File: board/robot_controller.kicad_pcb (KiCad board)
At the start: 2 copper layers, 171.4 x 142.6 mm, 328 parts, among them J101 +3.3V, J102 +24V, J103 GND, J104 JTAG-ARM, J105 Power, J106 FTDI-USB, J107 Industrial Inputs, J108 Industrial Outputs, J109 MCU-USB, J110 AUX-USART6, J111 UEXT0, J112 UEXT1, J113 RGB LEDs, J201 Temp 0, J2301 Motor 0, J2302 Limit 0, J2401 Motor 1, J2402 Limit 1, J2501 Motor 2, J2502 Limit 2, J2601 Motor 3, J2602 Limit 3, J301 Temp 1, Q101 PNP, Q1501 NJT4031NT1G, Q1601 NJT4031NT1G, Q1701 NJT4031NT1G, Q1801 NJT4031NT1G, Q1901 NJT4031NT1G, Q2001 NJT4031NT1G, Q2101 NJT4031NT1G, Q2201 NJT4031NT1G, Q401 MMBT5962, Q402 MMBT5962, Q501 MMBT5962, Q502 MMBT5962, SW101 SW0, SW102 SW1, SW103 SW2, SW104 SW3, SW105 RESET, SW106 BOOT, U101 STM32F405-144, U102 FT232RL, U201 MAX6675, U2301 L6470, U2401 L6470, U2501 L6470, U2601 L6470, U301 MAX6675, U601 LMZ14201, X101 8MHZ

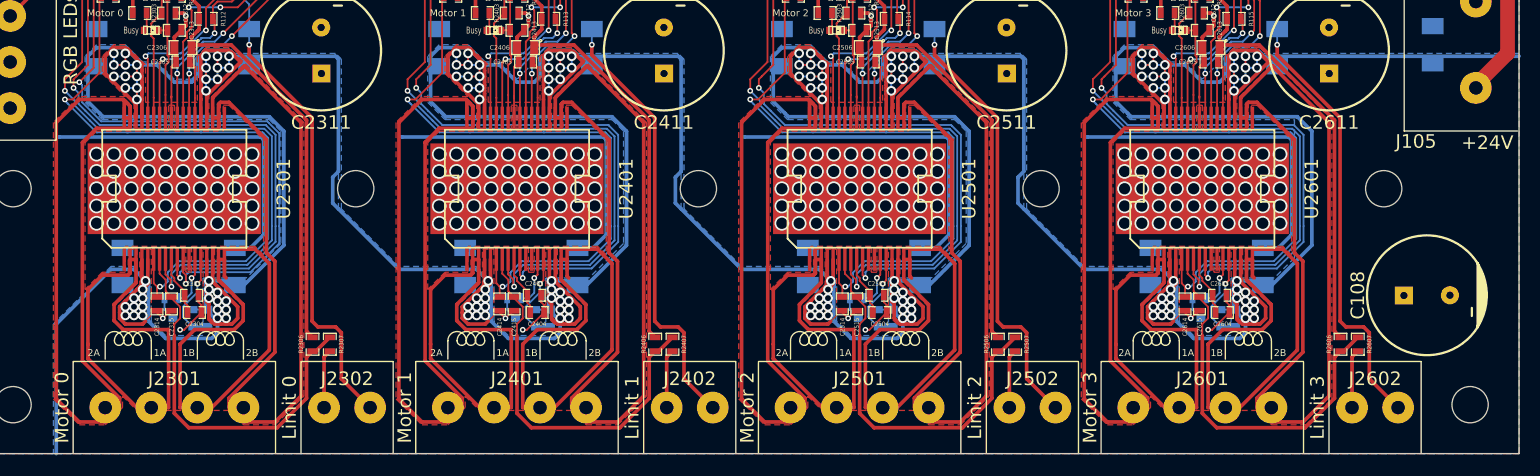
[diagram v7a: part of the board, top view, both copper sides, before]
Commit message: PentaLogix DRC Fixes
Moved some traces inside of the board outline.
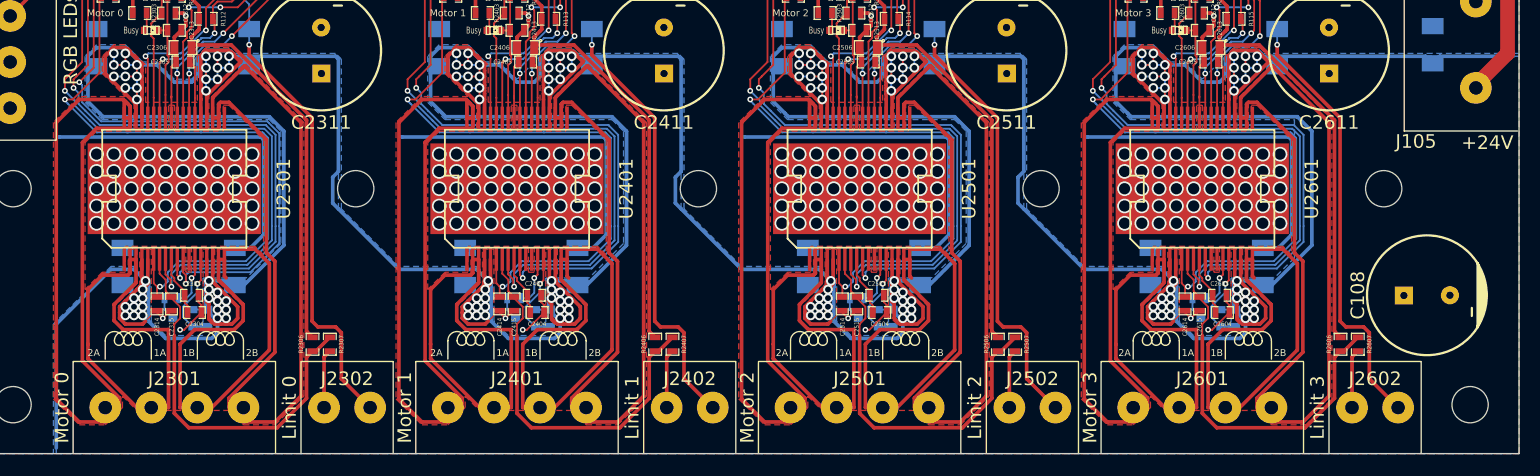
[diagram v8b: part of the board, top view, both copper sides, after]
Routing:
- net +24V: track 1244.9 -> 1244.3 mm
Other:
- rule pad_to_mask_clearance: 0.1016 -> 0.0254
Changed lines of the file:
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@@
-(kicad_pcb (version 3) (host pcbnew "(2014-02-15 BZR 4701)-product")
+(kicad_pcb (version 3) (host pcbnew "(2014-01-30 BZR 4648)-product")
   (general
     (links 796)
-    (no_connects 181)
-    (area -3.24213 15.8496 210.185001 162.46348)
+    (no_connects 0)
+    (area -3.24213 15.8496 208.98213 162.46348)
     (thickness 1.6)
     (drawings 59)
-    (tracks 4551)
+    (tracks 4554)
     (zones 0)
     (modules 328)
@@
   )
   (setup
-    (last_trace_width 0.2032)
+    (last_trace_width 0.4064)
     (user_trace_width 0.2032)
     (user_trace_width 0.4064)
@@
     (pad_size 0.635 1.143)
     (pad_drill 0)
-    (pad_to_mask_clearance 0.1016)
+    (pad_to_mask_clearance 0.0254)
     (aux_axis_origin 0 0)
     (visible_elements FFFFFF3F)
     (pcbplotparams
-      (layerselection 3178497)
-      (usegerberextensions true)
+      (layerselection 284196865)
+      (usegerberextensions false)
       (excludeedgelayer true)
       (linewidth 0.150000)
@@
       (drillshape 0)
       (scaleselection 1)
-      (outputdirectory ""))
+      (outputdirectory /home/andrew/board.gerber/))
   )
   (net 0 "")
@@
   (segment (start 62.23 106.68) (end 62.5475 106.68) (width 0.4064) (layer B.Cu) (net 0))
   (segment (start 140.0175 106.68) (end 140.97 106.68) (width 0.4064) (layer B.Cu) (net 0))
+  (segment (start 179.07 117.30228) (end 179.84978 116.5225) (width 0.4064) (layer B.Cu) (net 1) (status 400000))
+  (segment (start 179.84978 116.5225) (end 187.96 116.5225) (width 0.4064) (layer B.Cu) (net 1))
+  (segment (start 167.64 116.5225) (end 178.29022 116.5225) (width 0.4064) (layer B.Cu) (net 1))
+  (segment (start 178.29022 116.5225) (end 179.07 117.30228) (width 0.4064) (layer B.Cu) (net 1))
   (segment (start 125.73 50.165) (end 121.285 50.165) (width 0.8128) (layer B.Cu) (net 1))
   (via (at 111.4425 145.0975) (size 1.0668) (drill 0.635) (layers F.Cu B.Cu) (net 1))
@@
   (segment (start 160.3375 116.5225) (end 167.64 116.5225) (width 0.4064) (layer B.Cu) (net 1))
   (segment (start 167.6654 116.5225) (end 167.64 116.5225) (width 0.2032) (layer B.Cu) (net 1))
-  (segment (start 167.64 116.5225) (end 188.595 116.5225) (width 0.4064) (layer B.Cu) (net 1))
   (segment (start 118.4275 118.745) (end 117.7925 119.38) (width 0.4064) (layer B.Cu) (net 1))
   (segment (start 118.4275 116.84) (end 118.4275 118.745) (width 0.4064) (layer B.Cu) (net 1))
@@
   (segment (start 34.6075 140.0175) (end 35.8775 140.0175) (width 0.4064) (layer B.Cu) (net 1))
   (segment (start 33.3375 140.0175) (end 32.7025 140.6525) (width 0.4064) (layer B.Cu) (net 1))
-  (segment (start 27.305 146.05) (end 27.305 160.3375) (width 0.4064) (layer B.Cu) (net 1))
+  (segment (start 27.305 146.05) (end 27.305 159.7025) (width 0.4064) (layer B.Cu) (net 1))
   (segment (start 58.42 129.2225) (end 58.42 116.84) (width 0.4064) (layer B.Cu) (net 1))
   (segment (start 57.785 129.8575) (end 58.42 129.2225) (width 0.4064) (layer B.Cu) (net 1))
